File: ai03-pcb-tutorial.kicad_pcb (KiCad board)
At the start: 2 copper layers, 24 parts, among them SW1 SW_PUSH, U1 ATmega32U4-AU, Y1 16MHz

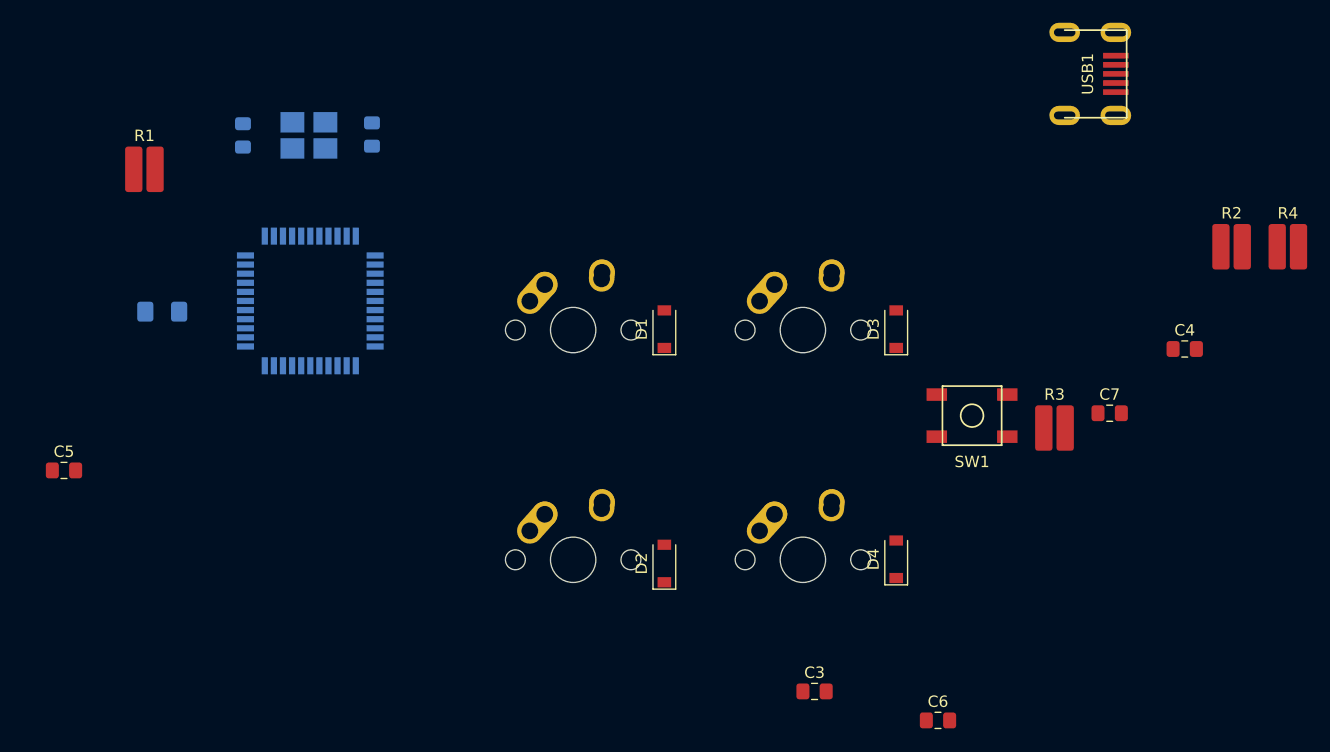
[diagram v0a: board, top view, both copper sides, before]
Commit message: set components position
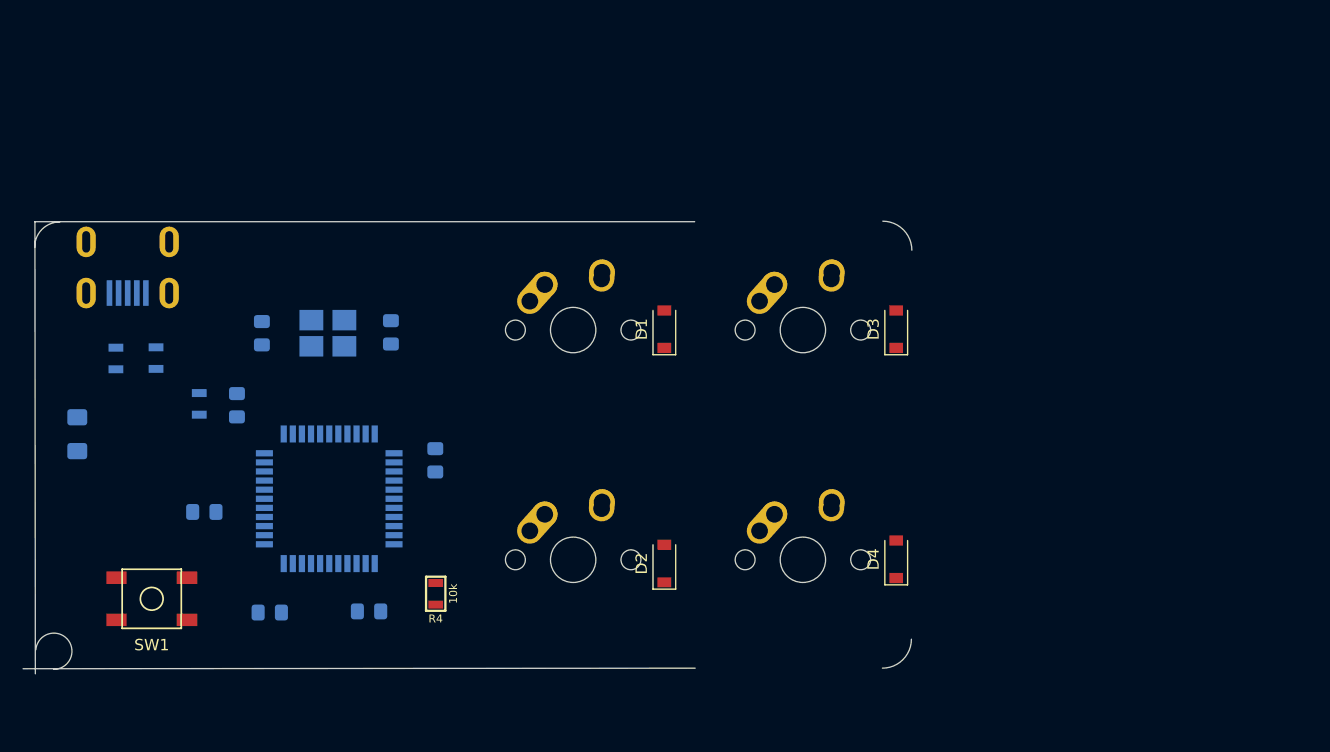
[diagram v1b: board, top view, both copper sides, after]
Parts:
- C3, C4, C5, C6, C7, USB1: moved to B.Cu
- R1, R2, R3: footprint Resistor_SMD:R_0815_2038Metric_Pad1.53x4.00mm_HandSolder -> Keebio-Parts:R_0805; moved to B.Cu
- R4: footprint Resistor_SMD:R_0815_2038Metric_Pad1.53x4.00mm_HandSolder -> Keebio-Parts:R_0805
- moved R2 95.1 mm to (23.2, 74.8), turned to 90 degrees
- moved USB1 83.7 mm to (20.7, 64.5), turned to 270 degrees
- moved C4 83.5 mm to (30.3, 78.9), turned to 90 degrees
- moved R3 82.8 mm to (19.7, 74.8), turned to 90 degrees
- moved R4 80.9 mm to (47.8, 95.5), turned to 90 degrees
- moved SW1 73.9 mm to (22.8, 95.9)
- moved C7 59.4 mm to (47.8, 83.8), turned to 90 degrees
- moved C3 55.9 mm to (27.4, 88.3), turned to 180 degrees
- moved C6 50.9 mm to (41.9, 97.0), turned to 180 degrees
- moved C5 22.0 mm to (33.2, 97.1)
- moved R1 21.2 mm to (27.0, 78.8), turned to 90 degrees
- moved U1 17.5 mm to (38.4, 87.1)
- moved C1 17.5 mm to (43.9, 72.5)
- moved C2 17.5 mm to (32.5, 72.6), turned to 90 degrees
- moved Y1 17.5 mm to (38.3, 72.6), turned to 180 degrees
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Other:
- board outline added: 78.2 x 39.8 mm

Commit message: draw edge line
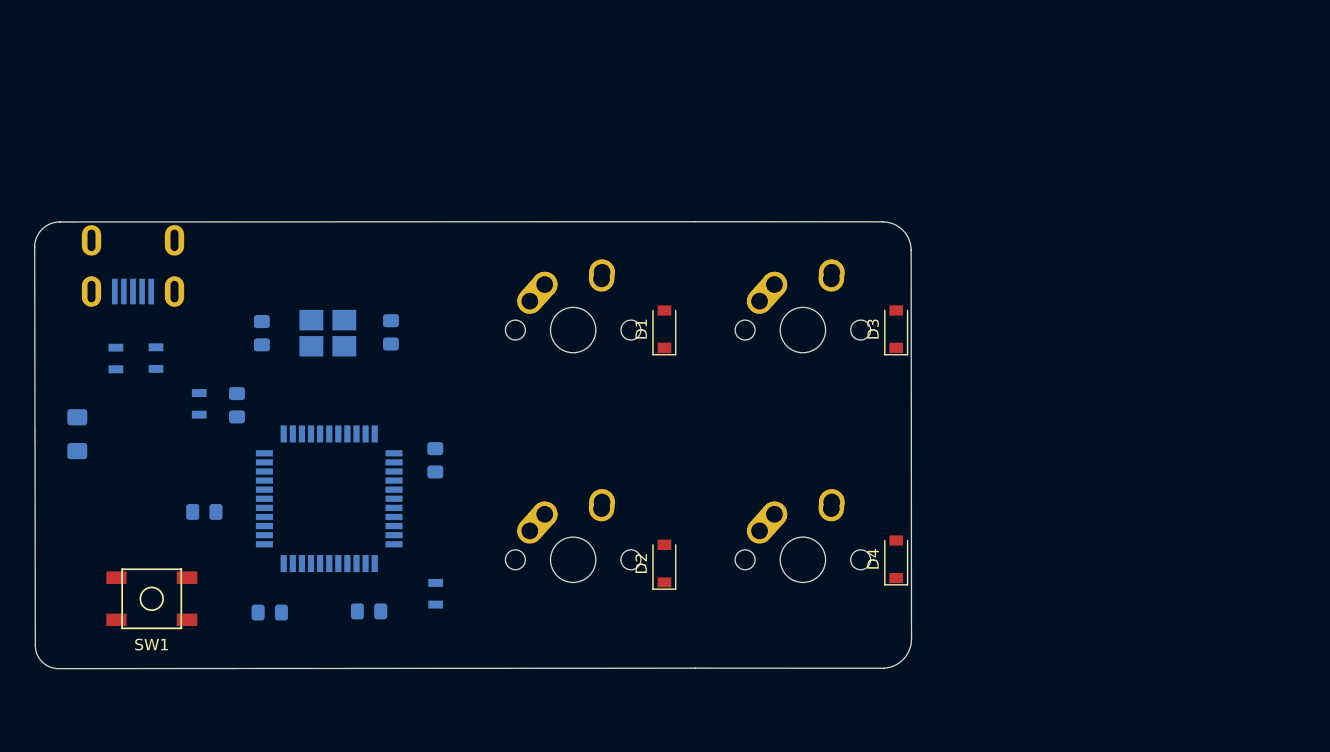
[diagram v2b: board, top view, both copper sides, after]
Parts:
- R4: moved to B.Cu
- moved USB1 0.49 mm to (21.2, 64.4)
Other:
- board size 78.2 x 39.8 mm -> 77.1 x 39.3 mm
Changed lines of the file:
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@@
   (general
     (thickness 1.6)
-    (drawings 7)
+    (drawings 10)
     (tracks 0)
     (zones 0)
@@
     (add_net VCC)
   )
-  (module Keebio-Parts:R_0805 (layer F.Cu)
+  (module Keebio-Parts:R_0805 (layer B.Cu)
     (at 47.79264 95.48876 90)
     (descr "SMT, 2012, 0805")
     (tags "SMT, 2012, 0805")
     (attr smd)
-    (fp_text reference R4 (at -2.2 0) (layer F.SilkS)
-      (effects (font (size 0.7 0.7) (thickness 0.15)))
-    )
-    (fp_text value 10k (at 0 1.55 90) (layer F.SilkS)
-      (effects (font (size 0.7 0.7) (thickness 0.15)))
-    )
-    (fp_line (start -1.5 0.85) (end 1.5 0.85) (layer F.SilkS) (width 0.2))
-    (fp_line (start -1.5 -0.85) (end -1.5 0.85) (layer F.SilkS) (width 0.2))
-    (fp_line (start 1.5 -0.85) (end 1.5 0.85) (layer F.SilkS) (width 0.2))
-    (fp_line (start -1.5 -0.85) (end 1.5 -0.85) (layer F.SilkS) (width 0.2))
-    (pad 1 smd rect (at -0.95 0 90) (size 0.7 1.3) (layers F.Cu F.Paste F.Mask)
+    (fp_text reference R4 (at -2.2 0) (layer B.SilkS)
+      (effects (font (size 0.7 0.7) (thickness 0.15)) (justify mirror))
+    )
+    (fp_text value 10k (at 0 -1.55 270) (layer B.SilkS)
+      (effects (font (size 0.7 0.7) (thickness 0.15)) (justify mirror))
+    )
+    (fp_line (start -1.5 0.85) (end 1.5 0.85) (layer B.SilkS) (width 0.2))
+    (fp_line (start 1.5 0.85) (end 1.5 -0.85) (layer B.SilkS) (width 0.2))
+    (fp_line (start -1.5 0.85) (end -1.5 -0.85) (layer B.SilkS) (width 0.2))
+    (fp_line (start -1.5 -0.85) (end 1.5 -0.85) (layer B.SilkS) (width 0.2))
+    (pad 2 smd rect (at 0.95 0 90) (size 0.7 1.3) (layers B.Cu B.Paste B.Mask)
+      (net 20 "Net-(R4-Pad2)") (clearance 0.1))
+    (pad 1 smd rect (at -0.95 0 90) (size 0.7 1.3) (layers B.Cu B.Paste B.Mask)
       (net 2 GND) (clearance 0.1))
-    (pad 2 smd rect (at 0.95 0 90) (size 0.7 1.3) (layers F.Cu F.Paste F.Mask)
-      (net 20 "Net-(R4-Pad2)") (clearance 0.1))
     (model ${KISYS3DMOD}/Resistor_SMD.3dshapes/R_0805_2012Metric.wrl
       (at (xyz 0 0 0))
@@
   )
   (module random-keyboard-parts:Molex-0548190589 (layer B.Cu)
-    (at 20.7086 64.54648 270)
+    (at 21.17852 64.4144 270)
     (attr smd)
     (fp_text reference USB1 (at 2.032 0) (layer B.SilkS)
@@
     )
   )
-  (gr_arc (start 14.21892 100.53828) (end 14.198601 102.128319) (angle -266.1582533) (layer Edge.Cuts) (width 0.05))
+  (gr_line (start 87.22868 102.03688) (end 70.612 102.0318) (layer Edge.Cuts) (width 0.05))
+  (gr_line (start 89.60104 65.26784) (end 89.631283 99.48672) (layer Edge.Cuts) (width 0.05))
+  (gr_line (start 70.57136 62.77356) (end 87.11184 62.7888) (layer Edge.Cuts) (width 0.05))
+  (gr_arc (start 14.615159 100.045519) (end 12.58824 100.03028) (angle -90.43078722) (layer Edge.Cuts) (width 0.05))
   (gr_arc (start 14.74216 65.00876) (end 14.74216 62.79388) (angle -90.94583496) (layer Edge.Cuts) (width 0.05))
-  (gr_line (start 70.612 102.0318) (end 11.5062 102.0826) (layer Edge.Cuts) (width 0.05))
-  (gr_line (start 12.55268 62.77356) (end 12.58824 102.52964) (layer Edge.Cuts) (width 0.05))
-  (gr_line (start 70.56628 62.77356) (end 12.55268 62.77356) (layer Edge.Cuts) (width 0.05))
-  (gr_arc (start 87.0712 99.48164) (end 87.0712 102.0318) (angle -90) (layer Edge.Cuts) (width 0.05))
-  (gr_arc (start 87.10676 65.28308) (end 89.662 65.28308) (angle -90) (layer Edge.Cuts) (width 0.05))
+  (gr_line (start 70.612 102.0318) (end 14.61008 102.07244) (layer Edge.Cuts) (width 0.05))
+  (gr_line (start 12.53236 64.9478) (end 12.58824 100.03536) (layer Edge.Cuts) (width 0.05))
+  (gr_line (start 70.56628 62.77356) (end 14.732 62.79896) (layer Edge.Cuts) (width 0.05))
+  (gr_arc (start 87.0712 99.48164) (end 87.22868 102.03688) (angle -86.35961693) (layer Edge.Cuts) (width 0.05))
+  (gr_arc (start 87.10676 65.28308) (end 89.60104 65.26784) (angle -89.64992831) (layer Edge.Cuts) (width 0.05))
 )

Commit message: reseet routing
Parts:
- moved R1 1.72 mm to (26.9, 80.5)
- moved C3 1.66 mm to (27.4, 86.6)
- moved R2 1.20 mm to (22.0, 74.7)
- moved F1 0.92 mm to (17.2, 81.2)
- moved R3 0.23 mm to (19.5, 74.7)
- turned SW1 to 180 degrees
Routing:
- net GND: track 0.00 -> 101.3 mm
- net +5V: track 0.00 -> 71.1 mm
- net Net-(R1-Pad1): track 0.00 -> 27.3 mm
- net Net-(R3-Pad1): track 0.00 -> 25.8 mm
- net Net-(R2-Pad1): track 0.00 -> 23.1 mm
- net Net-(C2-Pad2): track 0.00 -> 21.9 mm
- net Net-(C1-Pad2): track 0.00 -> 12.4 mm
- net VCC: track 0.00 -> 11.8 mm
- net Net-(R4-Pad2): track 0.00 -> 5.98 mm
- net D-: track 0.00 -> 5.19 mm
- net D+: track 0.00 -> 5.19 mm
- net Net-(C3-Pad1): track 0.00 -> 4.48 mm
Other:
- board size 77.1 x 39.3 mm -> 77.4 x 39.5 mm
- net class power added: clearance 0.2, trace_width 0.35, via_dia 0.8, via_drill 0.4

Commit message: re routing
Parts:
- SW1: moved to B.Cu
- moved C5 6.29 mm to (28.7, 92.7), turned to 270 degrees
- moved SW1 3.34 mm to (19.7, 97.0)
- moved C4 2.78 mm to (28.8, 76.6)
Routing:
- net ROW1: track 0.00 -> 96.2 mm, vias 0 -> 1
- net GND: track 101.3 -> 58.5 mm
- net ROW0: track 0.00 -> 33.1 mm, vias 0 -> 1
- net +5V: track 71.1 -> 52.1 mm
- net Net-(R1-Pad1): track 27.3 -> 17.4 mm, vias 0 -> 4
- net (no net): track 0.00 -> 0.80 mm

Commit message: adjust routeing
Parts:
- D1, D2, D3, D4: moved to B.Cu
- moved D3 30.1 mm to (60.5, 83.8), turned to 0 degrees
- moved MX2 28.5 mm to (80.0, 72.3)
- moved MX3 28.2 mm to (59.9, 92.0)
- moved D2 18.0 mm to (80.7, 80.2), turned to 0 degrees
- moved D4 11.7 mm to (80.5, 83.8), turned to 0 degrees
- moved D1 10.8 mm to (60.7, 80.2), turned to 0 degrees
- moved MX4 0.47 mm to (80.0, 92.0)
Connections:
- U1 pad 28: COL1 -> ROW1
- U1 pad 30: ROW1 -> COL1
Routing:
- net ROW1: track 96.2 -> 37.0 mm, vias 1 -> 0
- net COL1: track 0.00 -> 56.2 mm
- net COL0: track 0.00 -> 32.3 mm
- net Net-(D2-Pad2): track 0.00 -> 13.1 mm
- net Net-(D1-Pad2): track 0.00 -> 12.5 mm
- net Net-(R1-Pad1): track 17.4 -> 27.6 mm
- net ROW0: track 33.1 -> 38.7 mm, vias 1 -> 0
- net Net-(D3-Pad2): track 0.00 -> 3.82 mm
- net Net-(D4-Pad2): track 0.00 -> 3.37 mm
- net (no net): track 0.80 -> 0.00 mm

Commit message: reset edge line
reset edge line
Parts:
- moved D3 59.7 mm to (116.3, 62.6), turned to 90 degrees
- moved MX3 56.1 mm to (107.8, 62.9)
- moved C5 52.7 mm to (74.4, 66.5), turned to 90 degrees
- moved C2 39.4 mm to (69.6, 59.2), turned to 270 degrees
- moved D4 35.9 mm to (116.3, 82.5), turned to 90 degrees
- moved D1 35.4 mm to (96.0, 82.8), turned to 90 degrees
- moved R4 31.9 mm to (74.7, 78.2)
- moved R1 31.0 mm to (54.6, 66.5), turned to 270 degrees
- moved MX1 29.8 mm to (87.6, 83.1)
- moved U1 29.3 mm to (63.8, 72.5)
- moved MX4 29.2 mm to (107.8, 83.1)
- moved Y1 28.9 mm to (64.0, 59.2), turned to 0 degrees
- moved C3 26.8 mm to (50.5, 73.2), turned to 270 degrees
- moved C4 23.9 mm to (50.5, 66.5)
- moved D2 23.3 mm to (96.0, 62.6), turned to 90 degrees
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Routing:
- net COL1: track 56.2 -> 0.00 mm
- net ROW0: track 38.7 -> 0.00 mm
- net ROW1: track 37.0 -> 0.00 mm
- net +5V: track 52.1 -> 15.5 mm
- net COL0: track 32.3 -> 0.00 mm
- net Net-(R1-Pad1): track 27.6 -> 0.00 mm, vias 4 -> 0
- net Net-(D2-Pad2): track 13.1 -> 0.00 mm
- net Net-(D1-Pad2): track 12.5 -> 0.00 mm
- net Net-(C2-Pad2): track 21.9 -> 11.8 mm
- net Net-(C1-Pad2): track 12.4 -> 4.14 mm
- net Net-(R2-Pad1): track 23.1 -> 30.4 mm
- net Net-(R3-Pad1): track 25.8 -> 32.6 mm
- net GND: track 58.5 -> 52.5 mm
- net Net-(D3-Pad2): track 3.82 -> 0.00 mm
- net Net-(D4-Pad2): track 3.37 -> 0.00 mm
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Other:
- board size 77.4 x 39.5 mm -> 93.6 x 39.4 mm

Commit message: Ground fills
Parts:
- moved D3 30.2 mm to (88.6, 74.7), turned to 0 degrees
- moved D1 29.1 mm to (88.6, 54.6), turned to 0 degrees
- moved MX3 27.8 mm to (88.6, 83.1)
- moved MX1 20.2 mm to (88.6, 63.0)
- moved MX2 20.1 mm to (107.7, 63.0)
- moved C4 15.2 mm to (47.0, 81.3), turned to 0 degrees
- moved D2 14.2 mm to (107.7, 54.6), turned to 0 degrees
- moved D4 11.7 mm to (107.7, 74.7), turned to 0 degrees
- moved R1 1.78 mm to (52.8, 66.5)
- moved R2 0.51 mm to (34.8, 66.8)
- moved MX4 0.09 mm to (107.8, 83.1)
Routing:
- net GND: track 52.5 -> 156.0 mm, vias 0 -> 3
- net +5V: track 15.5 -> 91.9 mm
- net COL1: track 0.00 -> 62.0 mm
- net ROW0: track 0.00 -> 52.1 mm
- net Net-(R1-Pad1): track 0.00 -> 51.8 mm, vias 0 -> 2
- net ROW1: track 0.00 -> 43.5 mm
- net COL0: track 0.00 -> 38.4 mm
- net Net-(C1-Pad2): track 4.14 -> 16.6 mm, vias 0 -> 2
- net Net-(D4-Pad2): track 0.00 -> 5.66 mm
- net Net-(D2-Pad2): track 0.00 -> 5.61 mm
- net Net-(D1-Pad2): track 0.00 -> 4.23 mm
- net Net-(D3-Pad2): track 0.00 -> 3.67 mm
- added copper zone on B.Cu, net GND
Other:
- board text added: "4Switches"
